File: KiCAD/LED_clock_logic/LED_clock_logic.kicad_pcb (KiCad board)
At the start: 2 copper layers, 177.8 x 177.8 mm, 118 parts, among them J1 Socket, J10 Socket, J11 Socket, J12 Socket, J13 Socket, J14 Socket, J15 Socket, J16 Socket, J17 Socket, J18 Socket, J19 Socket, J2 Socket, J20 Socket, J21 Socket, J22 Socket, J23 Socket, J24 Socket, J25 Socket, J26 Socket, J27 Socket, J28 Socket, J29 Socket, J3 Socket, J30 Socket, J31 Socket, J32 Socket, J33 Socket, J34 Socket, J35 Socket, J36 Socket, J37 Socket, J38 Socket, J39 Socket, J4 Socket, J40 Socket, J41 Socket, J42 Socket, J43 Socket, J44 Socket, J45 Socket, J46 Socket, J47 Socket, J48 Socket, J49 Socket, J5 Socket, J50 Socket, J51 Socket, J52 Socket, J53 Socket, J54 Socket, J55 Socket, J56 Socket, J57 Socket, J58 Socket, J59 Socket, J6 Socket, J60 Socket, J61 Socket, J62 Socket, J63 Socket, J64 Socket, J65 Socket, J66 Socket, J67 Socket, J68 Socket, J69 Socket, J7 Socket, J70 Socket, J71 Socket, J72 Socket, J73 Socket, J74 Socket, J75 Socket, J76 Socket, J77 Socket, J78 Socket, J79 Socket, J8 Socket, J80 Socket, J81 Socket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

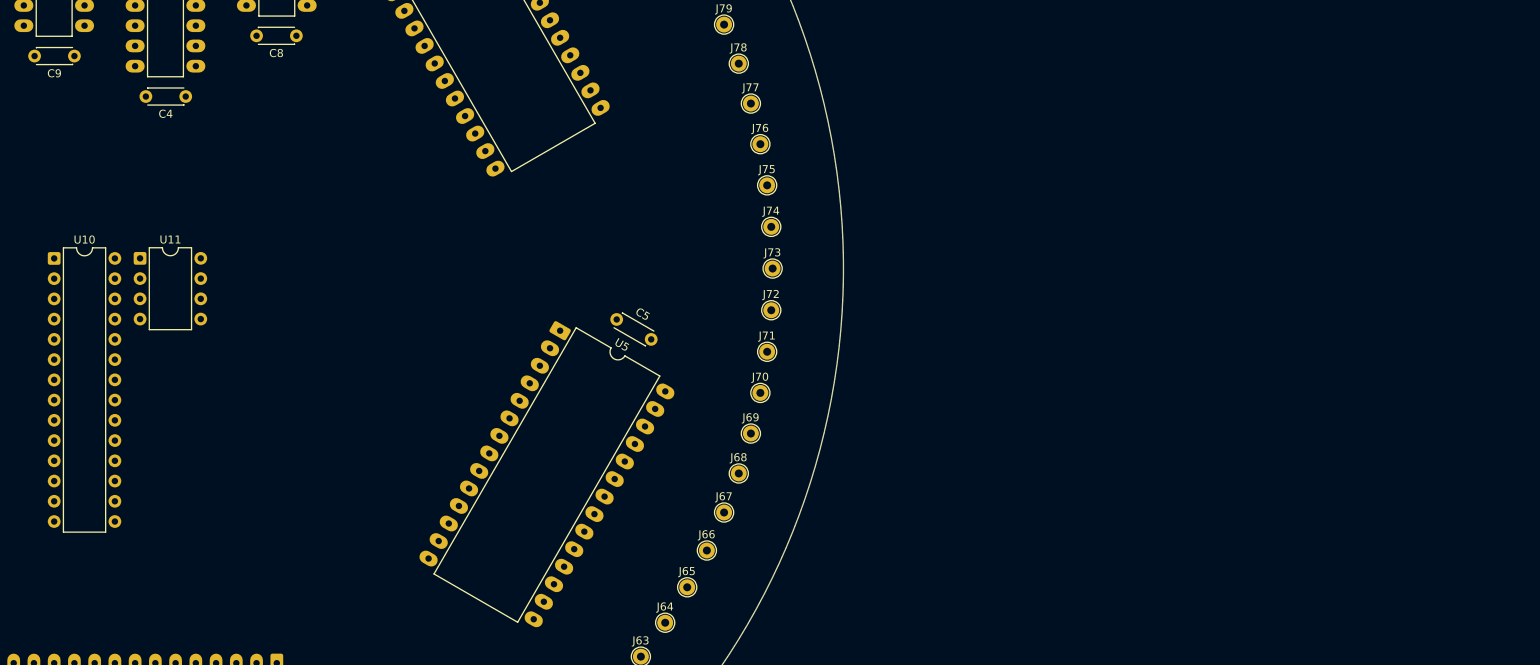
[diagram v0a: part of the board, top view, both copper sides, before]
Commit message: adding Z80
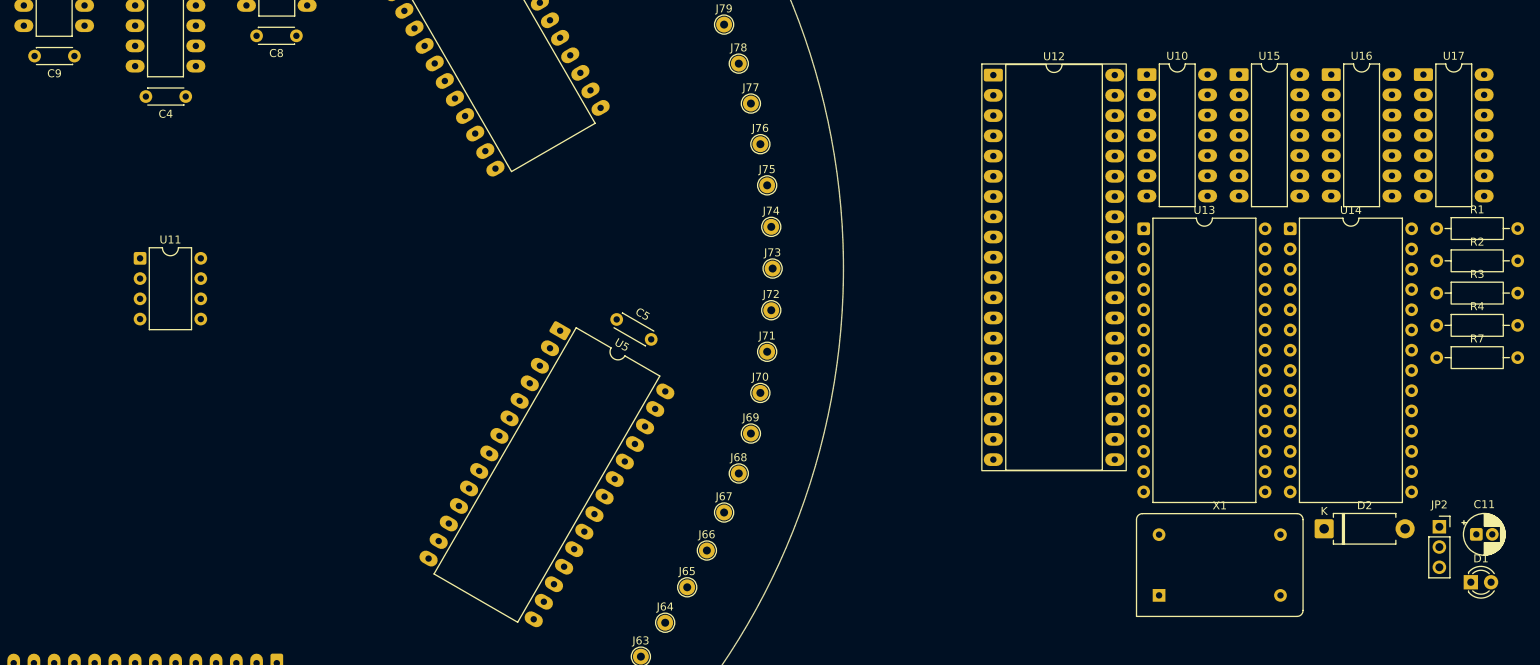
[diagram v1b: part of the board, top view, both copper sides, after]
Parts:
- added C11: 10uF, Capacitor_THT:CP_Radial_D5.0mm_P2.00mm, F.Cu at (422.3, 211.2)
- added D1: LED, LED_THT:LED_D3.0mm, F.Cu at (421.6, 217.2)
- added D2: 1N914, Diode_THT:D_DO-15_P10.16mm_Horizontal, F.Cu at (403.2, 210.5)
- added JP2: jpr3, Connector_PinSocket_2.54mm:PinSocket_1x03_P2.54mm_Vertical, F.Cu at (417.7, 210.2)
- added R1: 470, Resistor_THT:R_Axial_DIN0207_L6.3mm_D2.5mm_P10.16mm_Horizontal, F.Cu at (417.4, 172.8)
- added R2: 4.7k, Resistor_THT:R_Axial_DIN0207_L6.3mm_D2.5mm_P10.16mm_Horizontal, F.Cu at (417.4, 176.8)
- added R3: 1k, Resistor_THT:R_Axial_DIN0207_L6.3mm_D2.5mm_P10.16mm_Horizontal, F.Cu at (417.4, 180.9)
- added R4: 10k, Resistor_THT:R_Axial_DIN0207_L6.3mm_D2.5mm_P10.16mm_Horizontal, F.Cu at (417.4, 184.9)
- added R7: 4.7k, Resistor_THT:R_Axial_DIN0207_L6.3mm_D2.5mm_P10.16mm_Horizontal, F.Cu at (417.4, 189.0)
- added U12: Z80CPU, Package_DIP:DIP-40_W15.24mm_Socket_LongPads, F.Cu at (361.7, 153.5)
- added U13: AT28C256-15PU, Package_DIP:DIP-28_W15.24mm, F.Cu at (380.6, 172.8)
- added U14: AS6C62256-55PCN, Package_DIP:DIP-28_W15.24mm, F.Cu at (399.0, 172.8)
- added U15: 74LS32, Package_DIP:DIP-14_W7.62mm_LongPads, F.Cu at (392.6, 153.5)
- added U16: 74AS74, Package_DIP:DIP-14_W7.62mm_LongPads, F.Cu at (404.1, 153.5)
- added U17: 74AS74, Package_DIP:DIP-14_W7.62mm_LongPads, F.Cu at (415.7, 153.5)
- added X1: 20.000MHz, Oscillator:Oscillator_DIP-14, F.Cu at (382.5, 218.8)
- U10: value AVR128DB28x-xSP -> 74HC14; footprint Package_DIP:DIP-28_W7.62mm -> Package_DIP:DIP-14_W7.62mm_LongPads
- moved U10 139.1 mm to (381.0, 153.5)
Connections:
- U10 pad 1: unconnected-(U10-PA7-Pad1) -> Net-(D2-K)
- U10 pad 10: unconnected-(U10-PD4-Pad10) -> (no net)
- U10 pad 11: unconnected-(U10-PD5-Pad11) -> (no net)
- U10 pad 12: unconnected-(U10-PD6-Pad12) -> (no net)
- U10 pad 13: unconnected-(U10-VREFA/PD7-Pad13) -> (no net)
- U10 pad 14: unconnected-(U10-AVDD-Pad14) -> (no net)
- U10 pad 2: unconnected-(U10-PC0-Pad2) -> Net-(U10-Pad2)
- U10 pad 3: unconnected-(U10-PC1-Pad3) -> Net-(U10-Pad2)
- U10 pad 4: unconnected-(U10-PC2-Pad4) -> /nRST
- U10 pad 5: unconnected-(U10-PC3-Pad5) -> /A15
- U10 pad 6: unconnected-(U10-VDDIO2-Pad6) -> /nRAM
- U10 pad 7: unconnected-(U10-PD1-Pad7) -> (no net)
- U10 pad 8: unconnected-(U10-PD2-Pad8) -> Net-(D1-K)
- U10 pad 9: unconnected-(U10-PD3-Pad9) -> Net-(U12-~{HALT})
